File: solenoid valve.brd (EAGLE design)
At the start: 80 x 60 mm, 118 parts, among them CN1 8P8C-LED, IC1 IRFR320PBF, IC2 IRFR320PBF, IC3 IRFR320PBF, IC4 IRFR320PBF, IC5 IRFR320PBF, IC6 IRFR320PBF, IC7 IRFR320PBF, J1 XT30UPB-M, Q10 TLP291_SE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

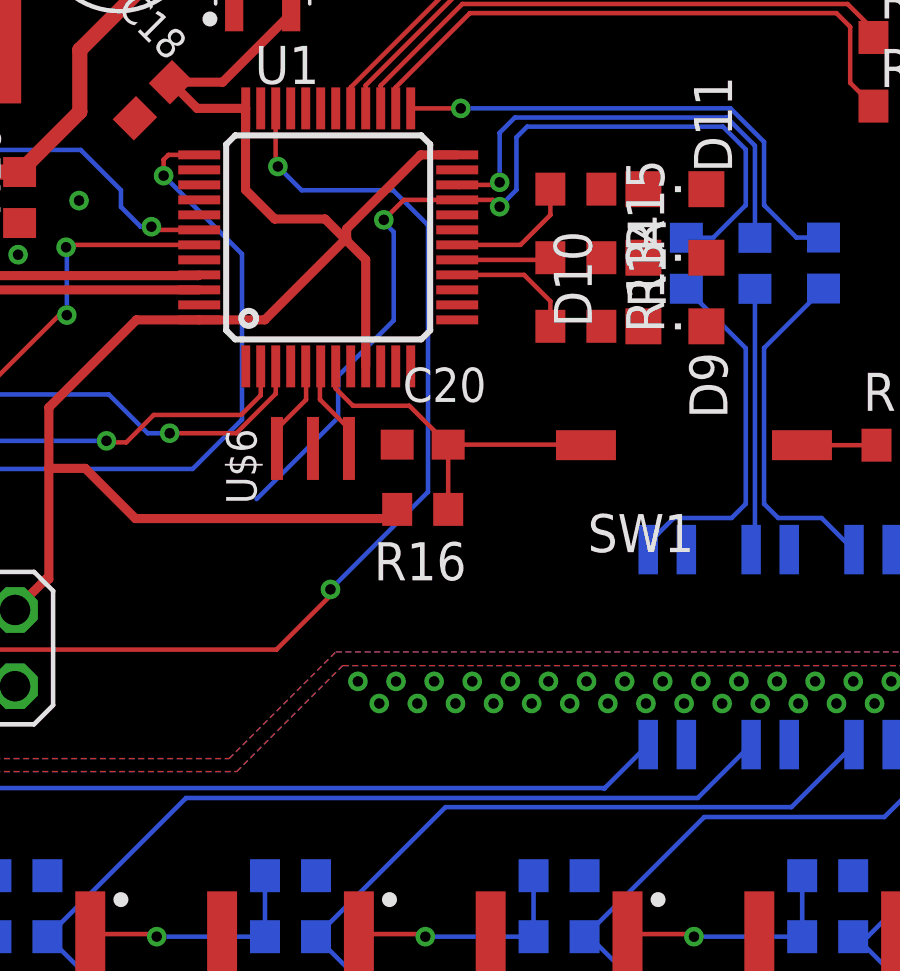
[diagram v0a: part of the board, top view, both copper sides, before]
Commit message: ERC and DRC check
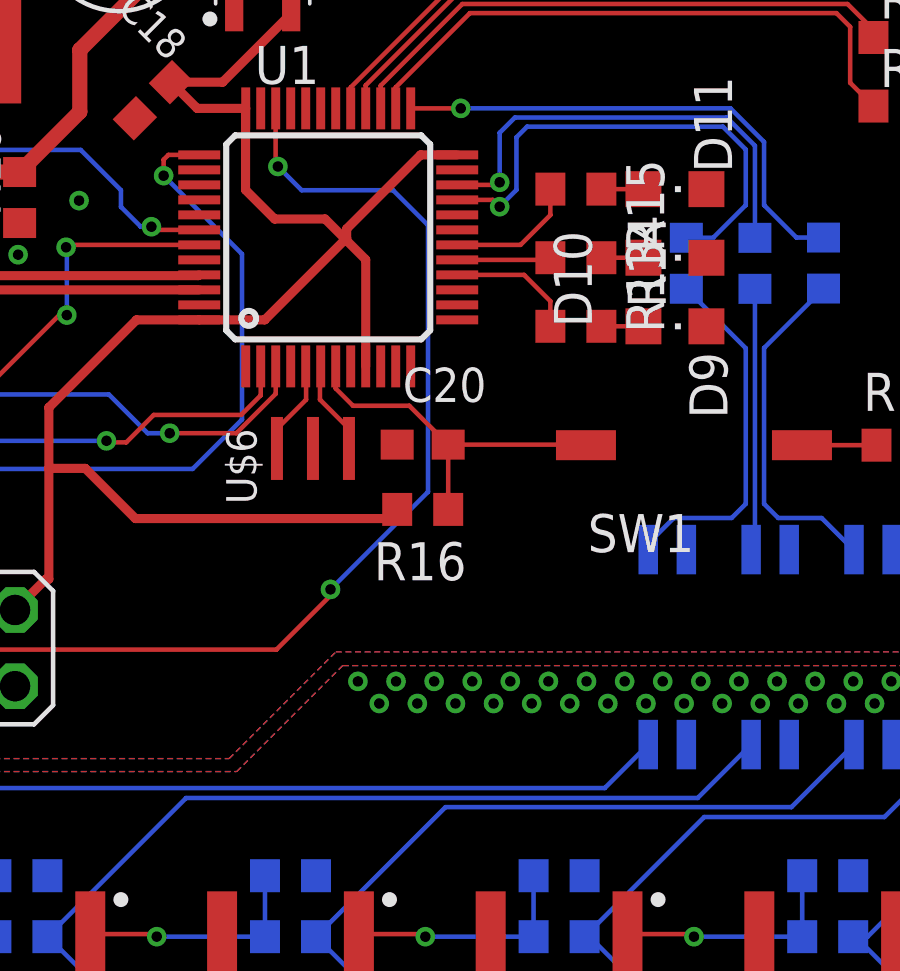
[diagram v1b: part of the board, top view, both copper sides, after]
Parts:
- C22: value (none) -> 100u
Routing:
- net SOLV0: track 30.5 -> 16.4 mm, vias 2 -> 1
- net N$9: track 0.00 -> 1.40 mm
- net N$21: track 0.00 -> 1.40 mm
- net N$10: track 0.00 -> 1.40 mm
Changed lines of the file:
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@@
 <attribute name="VALUE" x="30.8356" y="47.371" size="1.27" layer="27" rot="R90"/>
 </element>
-<element name="C22" library="rcl" library_urn="urn:adsk.eagle:library:334" package="E2-5" package3d_urn="urn:adsk.eagle:package:23346/2" value="" x="3.937" y="12.5984" smashed="yes" rot="R270">
+<element name="C22" library="rcl" library_urn="urn:adsk.eagle:library:334" package="E2-5" package3d_urn="urn:adsk.eagle:package:23346/2" value="100u" x="3.937" y="12.5984" smashed="yes" rot="R270">
 <attribute name="NAME" x="4.953" y="10.0584" size="1.27" layer="25" ratio="10" rot="R270"/>
 <attribute name="POPULARITY" value="14" x="3.937" y="12.5984" size="1.778" layer="27" rot="R270" display="off"/>
@@
 <contactref element="R14" pad="2"/>
 <contactref element="D10" pad="A"/>
-<wire x1="50.634" y1="45.9994" x2="52.036" y2="45.9994" width="0" layer="19" extent="1-1"/>
+<wire x1="50.634" y1="45.9994" x2="52.036" y2="45.9994" width="0.1524" layer="1"/>
 </signal>
 <signal name="N$10">
 <contactref element="R13" pad="2"/>
 <contactref element="D9" pad="A"/>
-<wire x1="50.634" y1="43.7134" x2="52.036" y2="43.7134" width="0" layer="19" extent="1-1"/>
+<wire x1="50.634" y1="43.7134" x2="52.036" y2="43.7134" width="0.1524" layer="1"/>
 </signal>
 <signal name="N$19">
@@
 <contactref element="D11" pad="A"/>
 <contactref element="R15" pad="2"/>
-<wire x1="50.634" y1="48.2854" x2="52.036" y2="48.2854" width="0" layer="19" extent="1-1"/>
+<wire x1="50.634" y1="48.2854" x2="52.036" y2="48.2854" width="0.1524" layer="1"/>
 </signal>
 <signal name="LED2">
 <contactref element="R15" pad="1"/>
 <contactref element="U1" pad="18"/>
-<wire x1="45.829" y1="46.4276" x2="45.8742" y2="46.4728" width="0.1524" layer="1"/>
 <wire x1="45.829" y1="46.4276" x2="47.9398" y2="46.4276" width="0.1524" layer="1"/>
 <wire x1="48.934" y1="47.4218" x2="48.934" y2="48.2854" width="0.1524" layer="1"/>
@@
 <contactref element="R13" pad="1"/>
 <contactref element="U1" pad="16"/>
-<wire x1="45.829" y1="45.4276" x2="45.8742" y2="45.4728" width="0.1524" layer="1"/>
 <wire x1="45.829" y1="45.4276" x2="48.058" y2="45.4276" width="0.1524" layer="1"/>
 <wire x1="48.934" y1="44.5516" x2="48.058" y2="45.4276" width="0.1524" layer="1"/>
@@
 <contactref element="R14" pad="1"/>
 <contactref element="U1" pad="17"/>
-<wire x1="45.829" y1="45.9276" x2="45.8742" y2="45.9728" width="0.1524" layer="1"/>
 <wire x1="45.829" y1="45.9276" x2="48.8622" y2="45.9276" width="0.1524" layer="1"/>
 <wire x1="48.8622" y1="45.9276" x2="48.934" y2="45.9994" width="0.1524" layer="1"/>
@@
 <signal name="SOLV1">
 <contactref element="U1" pad="22"/>
-<wire x1="45.890940625" y1="48.353146875" x2="45.829" y2="48.4150875" width="0.1524" layer="1"/>
-<wire x1="45.829" y1="48.4150875" x2="45.829" y2="48.4276" width="0.1524" layer="1"/>
 <contactref element="R6" pad="1"/>
 <via x="47.244" y="48.514" extent="1-16" drill="0.35"/>
-<wire x1="45.829" y1="48.4276" x2="47.1576" y2="48.4276" width="0.1524" layer="1"/>
-<wire x1="47.1576" y1="48.4276" x2="47.244" y2="48.514" width="0.1524" layer="1"/>
 <wire x1="47.244" y1="48.514" x2="47.244" y2="50.165" width="0.1524" layer="16"/>
 <wire x1="47.244" y1="50.165" x2="47.752" y2="50.673" width="0.1524" layer="16"/>
@@
 <wire x1="47.752" y1="50.673" x2="54.8124625" y2="50.673" width="0.1524" layer="16"/>
 <wire x1="55.753" y1="49.7324625" x2="55.753" y2="46.6614" width="0.1524" layer="16"/>
+<wire x1="47.244" y1="48.514" x2="47.1576" y2="48.4276" width="0.1524" layer="1"/>
+<wire x1="47.1576" y1="48.4276" x2="45.829" y2="48.4276" width="0.1524" layer="1"/>
 </signal>
 <signal name="SOLV3">
@@
 <signal name="SOLV0">
 <contactref element="U1" pad="21"/>
-<wire x1="41.86090625" y1="42.0576" x2="43.7134" y2="43.91009375" width="0.1524" layer="16"/>
-<wire x1="43.7134" y1="46.8554" x2="43.3832" y2="47.1856" width="0.1524" layer="16"/>
-<wire x1="43.3832" y1="47.2618" x2="43.3832" y2="47.1856" width="0.1524" layer="16"/>
-<wire x1="43.7134" y1="46.8554" x2="43.7134" y2="43.91009375" width="0.1524" layer="16"/>
-<via x="43.3832" y="47.2618" extent="1-16" drill="0.35"/>
-<wire x1="45.829" y1="47.9276" x2="44.049" y2="47.9276" width="0.1524" layer="1"/>
-<wire x1="43.3832" y1="47.2618" x2="44.049" y2="47.9276" width="0.1524" layer="1"/>
-<wire x1="39.1414" y1="37.9518" x2="41.86090625" y2="40.67130625" width="0.1524" layer="16"/>
-<wire x1="41.86090625" y1="40.67130625" x2="41.86090625" y2="42.0576" width="0.1524" layer="16"/>
 <contactref element="R27" pad="1"/>
 <via x="47.244" y="47.7012" extent="1-16" drill="0.35"/>
@@
 <contactref element="R28" pad="1"/>
 <wire x1="52.197" y1="29.77" x2="50.7486" y2="28.3216" width="0.1524" layer="16"/>
-<wire x1="50.7486" y1="28.3216" x2="50.7226" y2="28.2956" width="0.1524" layer="16"/>
 <wire x1="50.7486" y1="28.3216" x2="28.1683" y2="28.3216" width="0.1524" layer="16"/>
 <wire x1="28.1683" y1="28.3216" x2="23.24055" y2="23.39385" width="0.1524" layer="16"/>
